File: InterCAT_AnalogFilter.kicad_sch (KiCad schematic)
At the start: 25 parts, among them U3 TL082

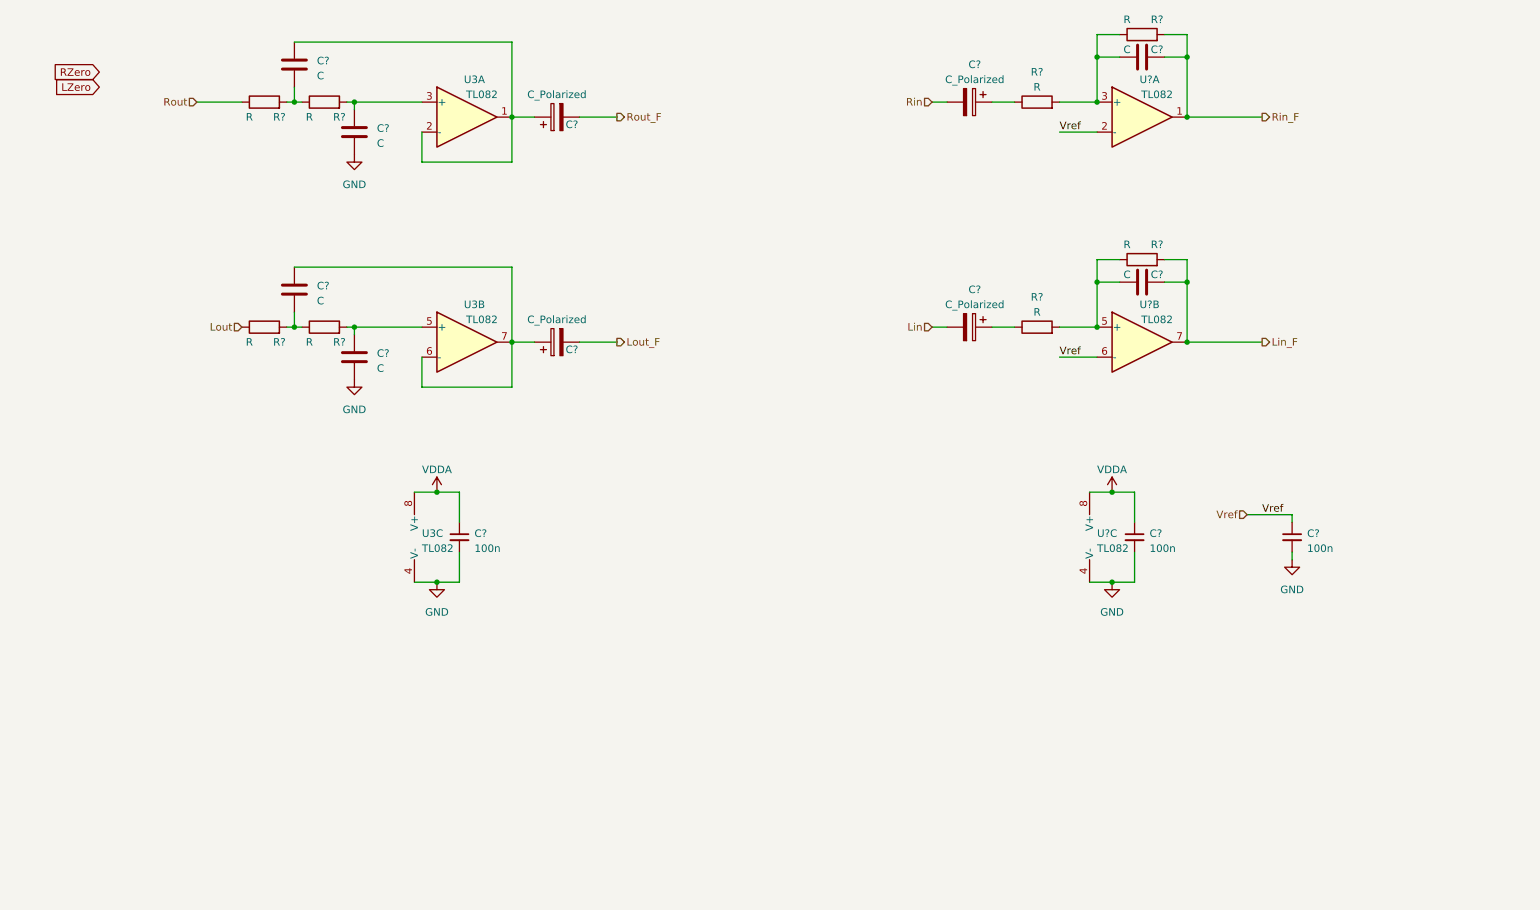
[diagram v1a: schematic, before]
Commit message: added trasf. on audio I/O added MAX3250 to library
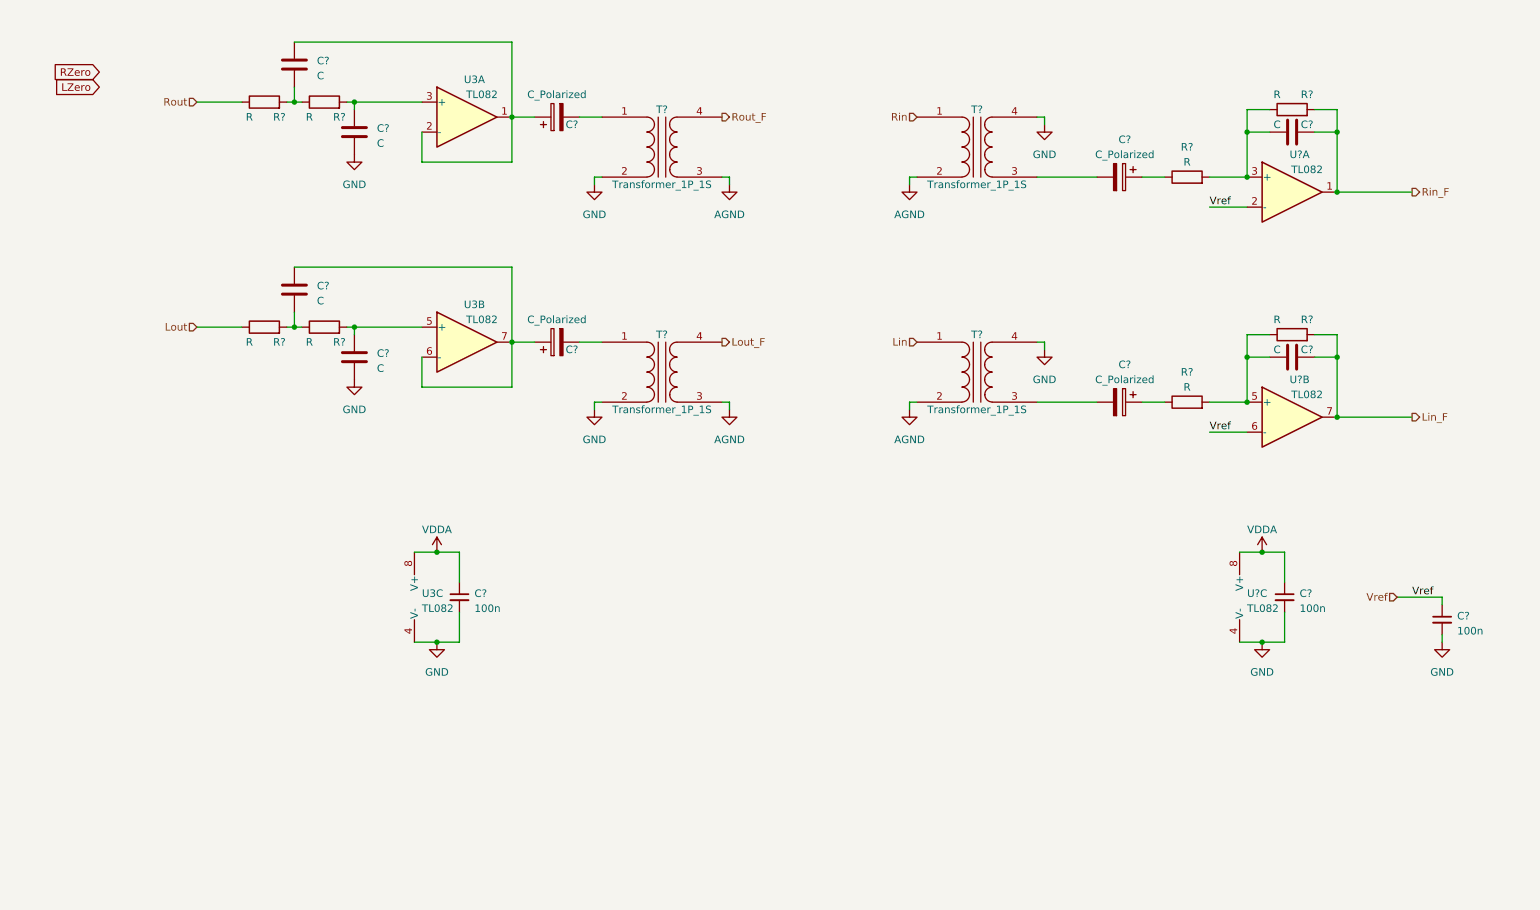
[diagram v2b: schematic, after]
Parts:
- added T? (x4): Transformer_1P_1S, symbol Device:Transformer_1P_1S
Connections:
- net GND: now also T?.2 (AB), T?.2 (AB), T?.2 (AB), T?.2 (AB), T?.3 (SA), T?.3 (SA), T?.4 (SB), T?.4 (SB)
- net Lin: now also T?.1 (AA); no longer C?.2
- net Lout_F: now also T?.4 (SB); no longer C?.2
- net Rin: now also T?.1 (AA); no longer C?.2
- net Rout_F: now also T?.4 (SB); no longer C?.2
- new net: C?.2, T?.3 (SA) (x2)
- new net: C?.2, T?.1 (AA) (x2)
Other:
- moved on the sheet: C?, R?, U3C, U?A, U?B, U?C

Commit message: first dimensioning of filters, library of MAX33251
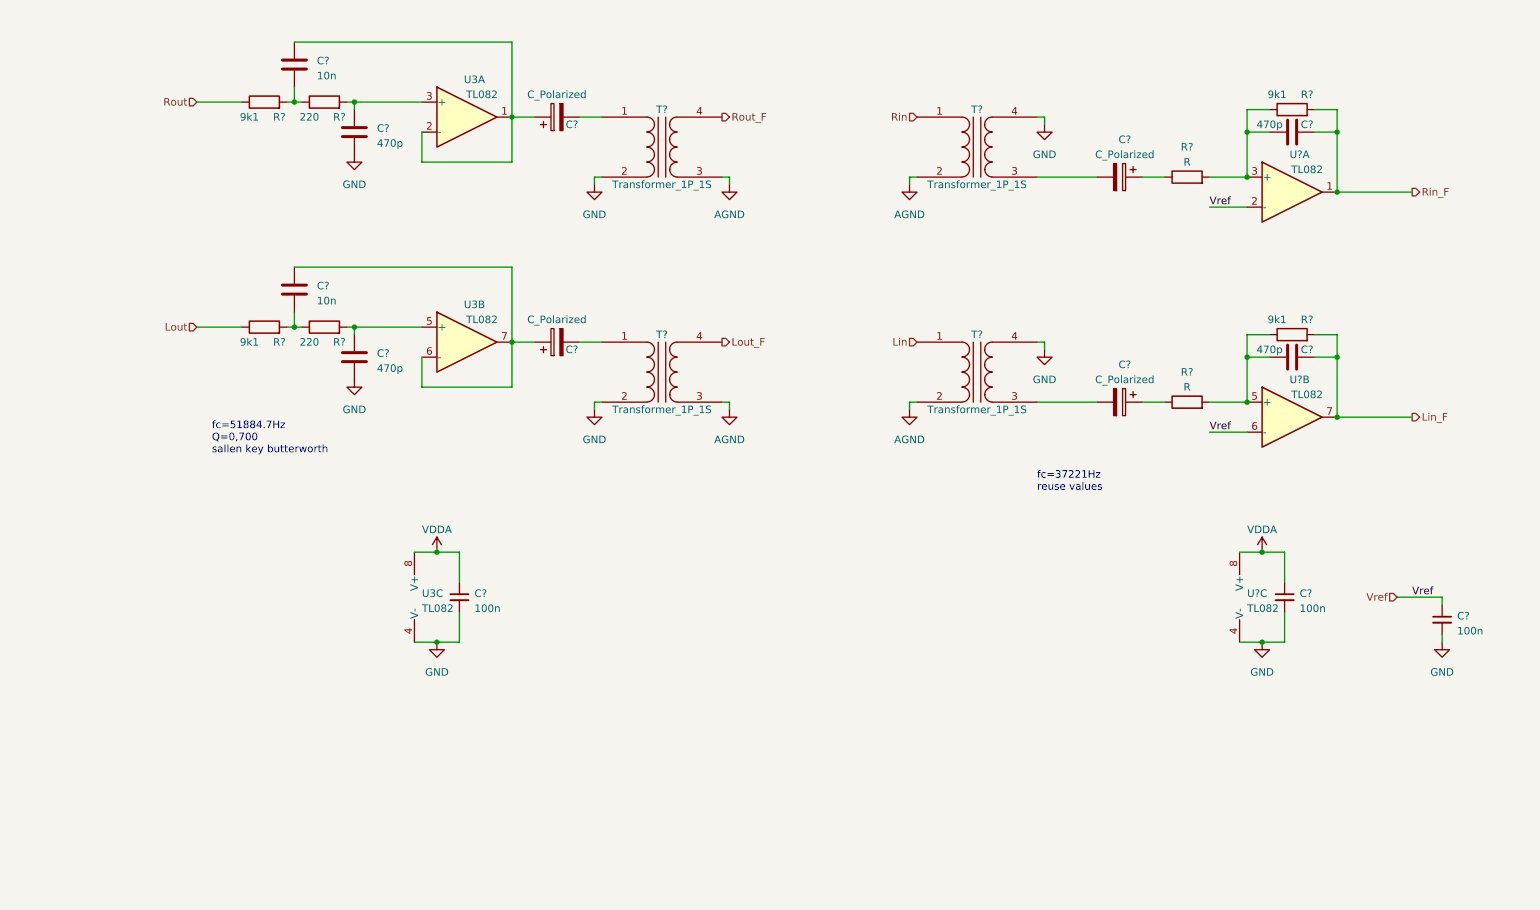
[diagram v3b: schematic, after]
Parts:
- removed C?: C, symbol Device:C
- added C?: 470p, symbol Device:C
- C? (x3): value C -> 470p
- C? (x2): value C -> 10n
- R? (x4): value R -> 9k1
- R? (x2): value R -> 220
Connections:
- net GND: now also C?.2
- net at R?.2, U3.5 (+): now also C?.1
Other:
- note added: "fc=37221Hz reuse values"
- note added: "fc=51884.7Hz Q=0,700 sallen key butterworth"
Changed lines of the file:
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@@
     (title "CAT_Interface")
     (date "2023-05-28")
-    (rev "1")
+    (rev "00")
     (company "ZX_Group")
     (comment 1 "made with <3 and KiCAD")
@@
     (stroke (width 0) (type default))
   )
+  (text "fc=37221Hz\nreuse values" (at 190.5 101.6 0)
+    (effects (font (size 1.27 1.27)) (justify left bottom))
+  )
+  (text "fc=51884.7Hz\nQ=0,700\nsallen key butterworth" (at 50.8 95.25 0)
+    (effects (font (size 1.27 1.27)) (justify left bottom))
+  )
   (label "Vref" (at 219.71 91.44 0) (fields_autoplaced)
     (effects (font (size 1.27 1.27)) (justify left bottom))
@@
     (effects (font (size 1.27 1.27)) (justify left bottom))
   )
-  (global_label "RZero" (shape input) (at 31.75 30.48 180) (fields_autoplaced)
-    (effects (font (size 1.27 1.27)) (justify right))
-    (property "Intersheetrefs" "${INTERSHEET_REFS}" (at 23.3409 30.48 0)
-      (effects (font (size 1.27 1.27)) (justify right) hide)
-    )
-  )
-  (global_label "LZero" (shape input) (at 31.75 33.02 180) (fields_autoplaced)
-    (effects (font (size 1.27 1.27)) (justify right))
-    (property "Intersheetrefs" "${INTERSHEET_REFS}" (at 23.5828 33.02 0)
-      (effects (font (size 1.27 1.27)) (justify right) hide)
-    )
-  )
   (hierarchical_label "Lin" (shape input) (at 170.18 76.2 180) (fields_autoplaced)
     (effects (font (size 1.27 1.27)) (justify right))
@@
       (effects (font (size 1.27 1.27)))
     )
-    (property "Value" "R" (at 57.15 38.1 90)
+    (property "Value" "9k1" (at 57.15 38.1 90)
       (effects (font (size 1.27 1.27)))
     )
@@
       (effects (font (size 1.27 1.27)))
     )
-    (property "Value" "R" (at 67.31 38.1 90)
+    (property "Value" "220" (at 67.31 38.1 90)
       (effects (font (size 1.27 1.27)))
     )
@@
       (effects (font (size 1.27 1.27)) (justify left))
     )
-    (property "Value" "C" (at 78.74 42.545 0)
+    (property "Value" "470p" (at 78.74 42.545 0)
       (effects (font (size 1.27 1.27)) (justify left))
     )
@@
       (effects (font (size 1.27 1.27)))
     )
-    (property "Value" "C" (at 231.14 39.37 90)
+    (property "Value" "470p" (at 229.87 39.37 90)
       (effects (font (size 1.27 1.27)))
     )
@@
       (effects (font (size 1.27 1.27)) (justify left))
     )
-    (property "Value" "C" (at 68.58 69.215 0)
+    (property "Value" "10n" (at 68.58 69.215 0)
       (effects (font (size 1.27 1.27)) (justify left))
     )
@@
       (effects (font (size 1.27 1.27)))
     )
-    (property "Value" "C" (at 231.14 77.47 90)
+    (property "Value" "470p" (at 229.87 77.47 90)
       (effects (font (size 1.27 1.27)))
     )
@@
       (effects (font (size 1.27 1.27)) (justify left))
     )
-    (property "Value" "C" (at 68.58 31.115 0)
+    (property "Value" "10n" (at 68.58 31.115 0)
       (effects (font (size 1.27 1.27)) (justify left))
     )
@@
       (effects (font (size 1.27 1.27)))
     )
-    (property "Value" "R" (at 67.31 76.2 90)
+    (property "Value" "220" (at 67.31 76.2 90)
       (effects (font (size 1.27 1.27)))
     )
@@
       (effects (font (size 1.27 1.27)) (justify left))
     )
-    (property "Value" "C" (at 78.74 80.645 0)
+    (property "Value" "470p" (at 78.74 80.645 0)
       (effects (font (size 1.27 1.27)) (justify left))
     )
@@
       (effects (font (size 1.27 1.27)))
     )
-    (property "Value" "R" (at 57.15 76.2 90)
+    (property "Value" "9k1" (at 57.15 76.2 90)
       (effects (font (size 1.27 1.27)))
     )
@@
       (effects (font (size 1.27 1.27)))
     )
-    (property "Value" "R" (at 231.14 34.29 90)
+    (property "Value" "9k1" (at 231.14 34.29 90)
       (effects (font (size 1.27 1.27)))
     )
@@
       (effects (font (size 1.27 1.27)))
     )
-    (property "Value" "R" (at 231.14 72.39 90)
-      (effects (font (size 1.27 1.27)))
-    )
+    (property "Value" "9k1" (at 231.14 72.39 90)
+      (effects (font (size 1.27 1.27)))
+    )

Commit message: changed analog filters, added gain
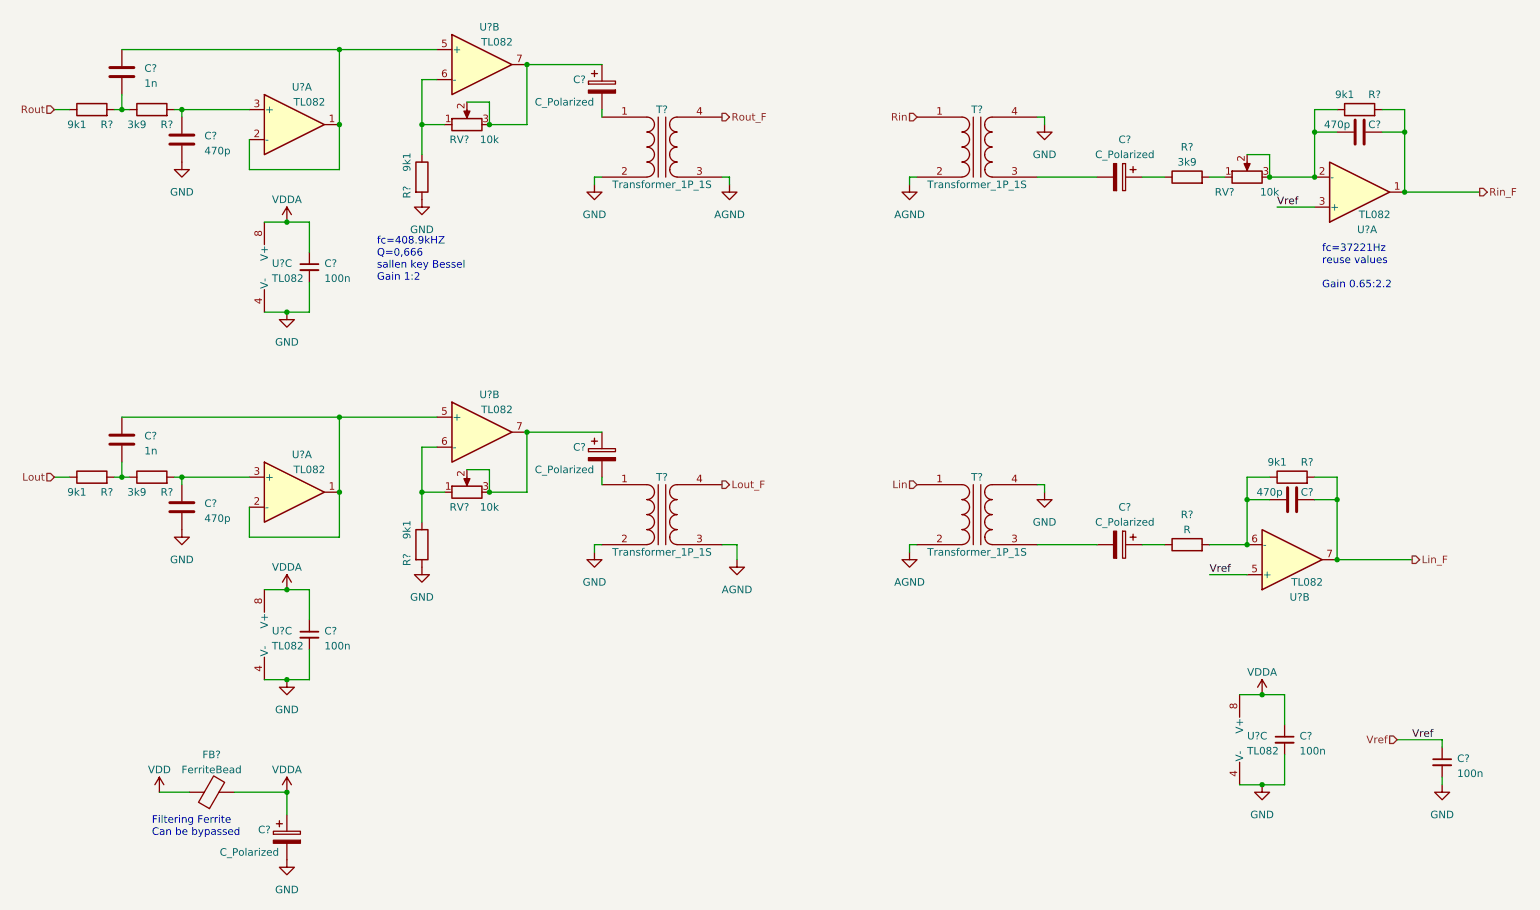
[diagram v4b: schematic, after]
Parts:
- removed C?: 10n, symbol Device:C
- removed C?: C_Polarized, symbol Device:C_Polarized
- removed C?: 470p, symbol Device:C
- removed R?: 220, symbol Device:R
- removed R?: 9k1, symbol Device:R
- removed T?: Transformer_1P_1S, symbol Device:Transformer_1P_1S
- removed unit 2 of U3
- added C?: 100n, symbol Device:C_Small
- added C? (x2): C_Polarized, symbol Device:C_Polarized
- added C?: 1n, symbol Device:C
- added C?: 470p, symbol Device:C
- added FB?: FerriteBead, symbol Device:FerriteBead
- added R?: 3k9, symbol Device:R
- added R? (x3): 9k1, symbol Device:R
- added RV? (x3): 10k, symbol Device:R_Potentiometer
- added T?: Transformer_1P_1S, symbol Device:Transformer_1P_1S
- added U? (x4): TL082, symbol Amplifier_Operational:TL082
- C?: value 10n -> 1n
- R?: value 220 -> 3k9
- R?: value R -> 3k9
- renumbered U3 to U?
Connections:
- net GND: now also C?.2, C?.2, C?.2, R?.2, R?.2, T?.2 (AB), T?.3 (SA), U?.4 (V-)
- net Lout: now also R?.1
- net Lout_F: now also T?.4 (SB)
- net VDD: now also C?.1, C?.1, FB?.1, FB?.2, U?.8 (V+)
- net Vref: now also U?.3 (+), U?.5 (+); no longer U?.2 (-), U?.6 (-)
- net at C?.1, R?.1: now also U?.2 (-), RV?.2, RV?.3; no longer R?.2, U?.3 (+)
- net at C?.1, U?.1, U?.2 (-): now also U?.5 (+); no longer C?.1
- net at C?.1, R?.1, R?.2: now also U?.6 (-); no longer U?.5 (+)
- new net: C?.1, U?.1, U?.2 (-), U?.5 (+)
- new net: C?.1, R?.2, U?.3 (+)
- new net: R?.2, RV?.1
- new net: C?.1, RV?.2, RV?.3, U?.7 (x2)
- new net: C?.2, T?.1 (AA)
- new net: C?.2, R?.1, R?.2
- new net: R?.1, RV?.1, U?.6 (-) (x2)
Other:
- note added: "Filtering Ferrite Can be bypassed"
- note added: "fc=37221Hz reuse values Gain 0.65:2.2"
- note added: "fc=408.9kHZ Q=0,666 sallen key Bessel Gain 1:2"
- note removed: "fc=37221Hz reuse values"
- note removed: "fc=51884.7Hz Q=0,700 sallen key butterworth"
- moved on the sheet: C?, R?, T?, U?A, U?B, U?C
